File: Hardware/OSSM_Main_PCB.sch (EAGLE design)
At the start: 11 parts, among them J1 PJ-037AH, U1 LOLIN32_PRODUCTION

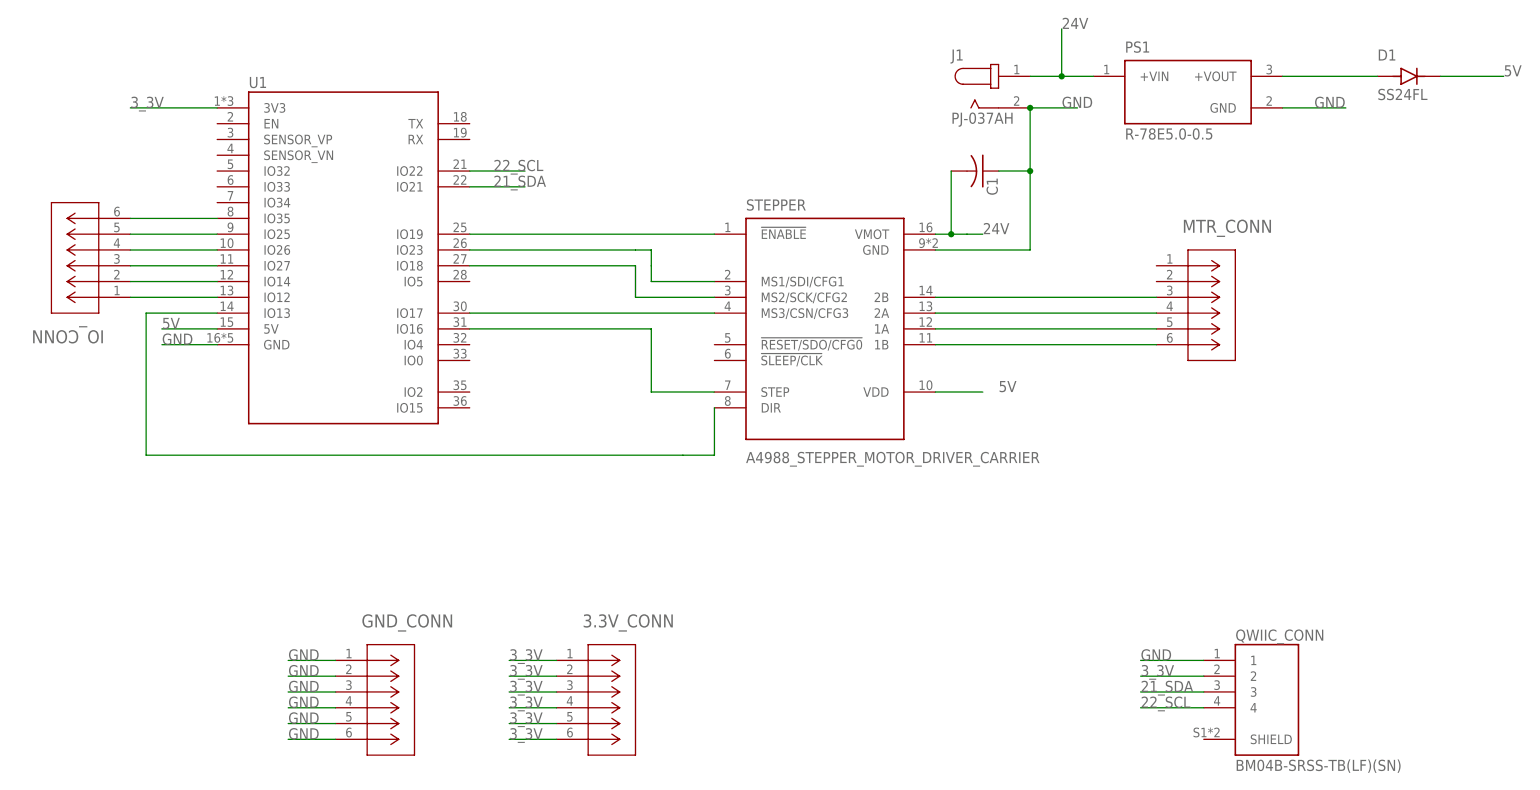
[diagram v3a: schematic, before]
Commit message: Added holes, fixed 3.3V VIO
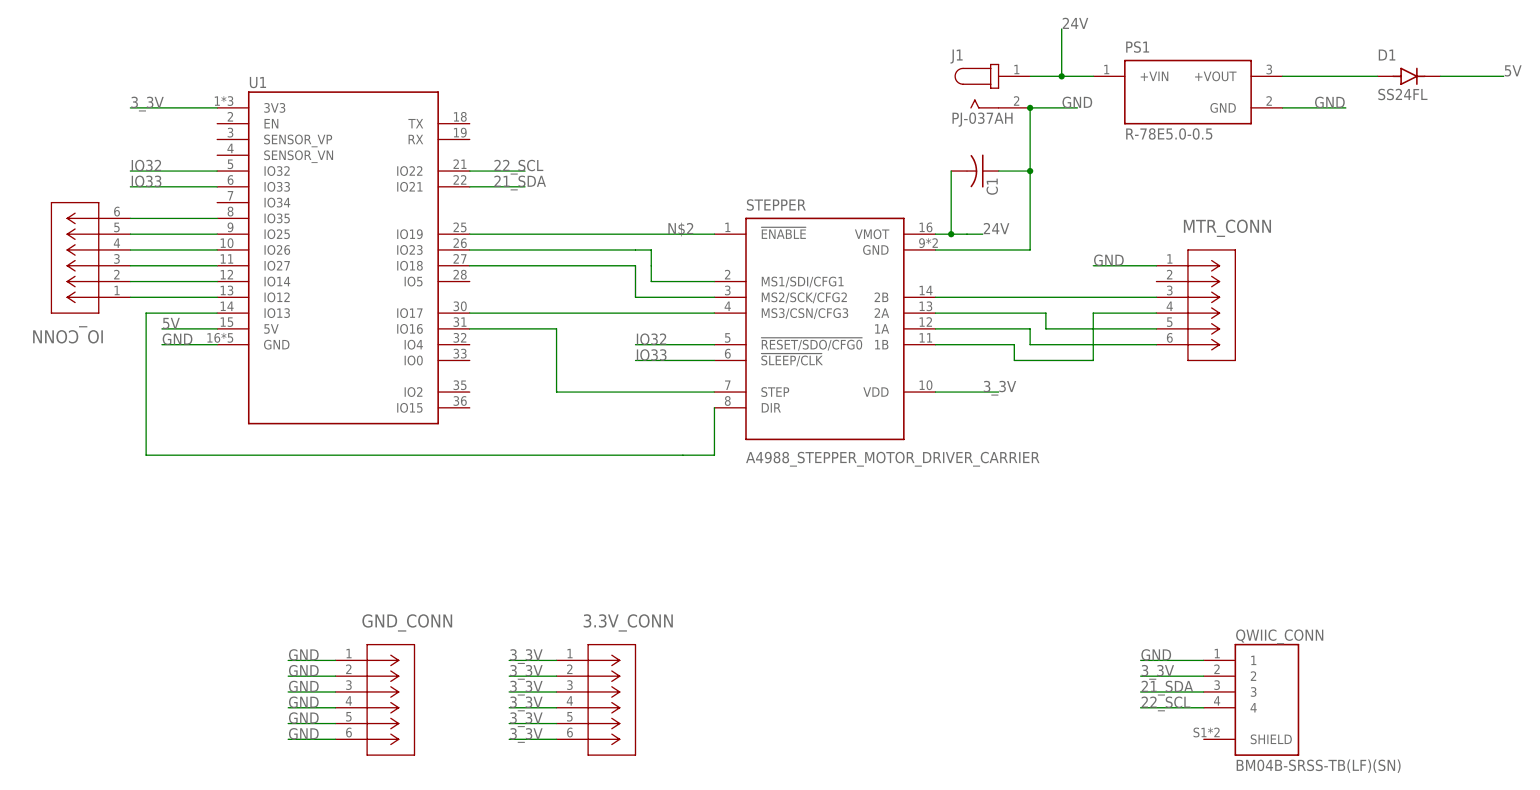
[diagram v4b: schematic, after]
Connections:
- new net IO32: STEPPER.!RESET/SDO/CFG0, U1.IO32
- new net IO33: STEPPER.!SLEEP/CLK, U1.IO33
- net 3_3V: now also STEPPER.VDD
- net 5V: no longer STEPPER.VDD
- net GND: now also MTR_CONN.1
- net N$10: now also STEPPER.1B; no longer STEPPER.2A
- net N$8: now also STEPPER.1A; no longer STEPPER.1B
- net N$9: now also STEPPER.2A; no longer STEPPER.1A
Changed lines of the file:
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@@
 <?xml version="1.0" encoding="utf-8"?>
 <!DOCTYPE eagle SYSTEM "eagle.dtd">
-<eagle version="9.6.2">
+<eagle version="9.6.1">
 <drawing>
 <settings>
@@
 <label x="213.36" y="154.94" size="1.778" layer="95"/>
 </segment>
+<segment>
+<pinref part="MTR_CONN" gate="A" pin="1"/>
+<wire x1="187.96" y1="129.54" x2="177.8" y2="129.54" width="0.1524" layer="91"/>
+<label x="177.8" y="129.54" size="1.778" layer="95"/>
+</segment>
 </net>
 <net name="3_3V" class="0">
@@
 <wire x1="36.83" y1="154.94" x2="22.86" y2="154.94" width="0.1524" layer="91"/>
 <label x="22.86" y="154.94" size="1.778" layer="95"/>
+</segment>
+<segment>
+<pinref part="STEPPER" gate="G$1" pin="VDD"/>
+<wire x1="152.4" y1="109.22" x2="162.56" y2="109.22" width="0.1524" layer="91"/>
+<label x="160.02" y="109.22" size="1.778" layer="95"/>
 </segment>
 </net>
@@
 <label x="27.94" y="119.38" size="1.778" layer="95"/>
 </segment>
-<segment>
-<pinref part="STEPPER" gate="G$1" pin="VDD"/>
-<wire x1="152.4" y1="109.22" x2="160.02" y2="109.22" width="0.1524" layer="91"/>
-<label x="162.56" y="109.22" size="1.778" layer="95"/>
-</segment>
 </net>
 <net name="N$2" class="0">
@@
 <pinref part="STEPPER" gate="G$1" pin="!ENABLE"/>
 <wire x1="77.47" y1="134.62" x2="116.84" y2="134.62" width="0.1524" layer="91"/>
+<label x="109.22" y="134.62" size="1.778" layer="95"/>
 </segment>
 </net>
@@
 <segment>
 <pinref part="U1" gate="G$1" pin="IO16"/>
-<wire x1="77.47" y1="119.38" x2="106.68" y2="119.38" width="0.1524" layer="91"/>
+<wire x1="77.47" y1="119.38" x2="91.44" y2="119.38" width="0.1524" layer="91"/>
 <pinref part="STEPPER" gate="G$1" pin="STEP"/>
-<wire x1="106.68" y1="119.38" x2="106.68" y2="109.22" width="0.1524" layer="91"/>
-<wire x1="106.68" y1="109.22" x2="116.84" y2="109.22" width="0.1524" layer="91"/>
+<wire x1="91.44" y1="119.38" x2="91.44" y2="109.22" width="0.1524" layer="91"/>
+<wire x1="91.44" y1="109.22" x2="116.84" y2="109.22" width="0.1524" layer="91"/>
 </segment>
 </net>
@@
 </segment>
 </net>
-<net name="N$8" class="0">
-<segment>
-<pinref part="STEPPER" gate="G$1" pin="1B"/>
-<pinref part="MTR_CONN" gate="A" pin="6"/>
-<wire x1="152.4" y1="116.84" x2="187.96" y2="116.84" width="0.1524" layer="91"/>
-</segment>
-</net>
-<net name="N$9" class="0">
-<segment>
-<pinref part="MTR_CONN" gate="A" pin="5"/>
-<pinref part="STEPPER" gate="G$1" pin="1A"/>
-<wire x1="187.96" y1="119.38" x2="152.4" y2="119.38" width="0.1524" layer="91"/>
-</segment>
-</net>
-<net name="N$10" class="0">
-<segment>
-<pinref part="STEPPER" gate="G$1" pin="2A"/>
-<pinref part="MTR_CONN" gate="A" pin="4"/>
-<wire x1="152.4" y1="121.92" x2="187.96" y2="121.92" width="0.1524" layer="91"/>
-</segment>
-</net>
 <net name="N$11" class="0">
 <segment>
@@
 </segment>
 </net>
+<net name="IO33" class="0">
+<segment>
+<pinref part="U1" gate="G$1" pin="IO33"/>
+<wire x1="36.83" y1="142.24" x2="22.86" y2="142.24" width="0.1524" layer="91"/>
+<label x="22.86" y="142.24" size="1.778" layer="95"/>
+</segment>
+<segment>
+<pinref part="STEPPER" gate="G$1" pin="!SLEEP/CLK"/>
+<wire x1="116.84" y1="114.3" x2="104.14" y2="114.3" width="0.1524" layer="91"/>
+<label x="104.14" y="114.3" size="1.778" layer="95"/>
+</segment>
+</net>
+<net name="IO32" class="0">
+<segment>
+<pinref part="U1" gate="G$1" pin="IO32"/>
+<wire x1="36.83" y1="144.78" x2="22.86" y2="144.78" width="0.1524" layer="91"/>
+<label x="22.86" y="144.78" size="1.778" layer="95"/>
+</segment>
+<segment>
+<pinref part="STEPPER" gate="G$1" pin="!RESET/SDO/CFG0"/>
+<wire x1="116.84" y1="116.84" x2="104.14" y2="116.84" width="0.1524" layer="91"/>
+<label x="104.14" y="116.84" size="1.778" layer="95"/>
+</segment>
+</net>
+<net name="N$8" class="0">
+<segment>
+<pinref part="STEPPER" gate="G$1" pin="1A"/>
+<wire x1="152.4" y1="119.38" x2="167.64" y2="119.38" width="0.1524" layer="91"/>
+<wire x1="167.64" y1="119.38" x2="167.64" y2="116.84" width="0.1524" layer="91"/>
+<pinref part="MTR_CONN" gate="A" pin="6"/>
+<wire x1="167.64" y1="116.84" x2="187.96" y2="116.84" width="0.1524" layer="91"/>
+</segment>
+</net>
+<net name="N$9" class="0">
+<segment>
+<pinref part="STEPPER" gate="G$1" pin="2A"/>
+<wire x1="152.4" y1="121.92" x2="170.18" y2="121.92" width="0.1524" layer="91"/>
+<wire x1="170.18" y1="121.92" x2="170.18" y2="119.38" width="0.1524" layer="91"/>
+<pinref part="MTR_CONN" gate="A" pin="5"/>
+<wire x1="170.18" y1="119.38" x2="187.96" y2="119.38" width="0.1524" layer="91"/>
+</segment>
+</net>
+<net name="N$10" class="0">
+<segment>
+<wire x1="177.8" y1="114.3" x2="177.8" y2="121.92" width="0.1524" layer="91"/>
+<pinref part="MTR_CONN" gate="A" pin="4"/>
+<wire x1="177.8" y1="121.92" x2="187.96" y2="121.92" width="0.1524" layer="91"/>
+<pinref part="STEPPER" gate="G$1" pin="1B"/>
+<wire x1="152.4" y1="116.84" x2="165.1" y2="116.84" width="0.1524" layer="91"/>
+<wire x1="165.1" y1="116.84" x2="165.1" y2="114.3" width="0.1524" layer="91"/>
+<wire x1="165.1" y1="114.3" x2="177.8" y2="114.3" width="0.1524" layer="91"/>
+</segment>
+</net>

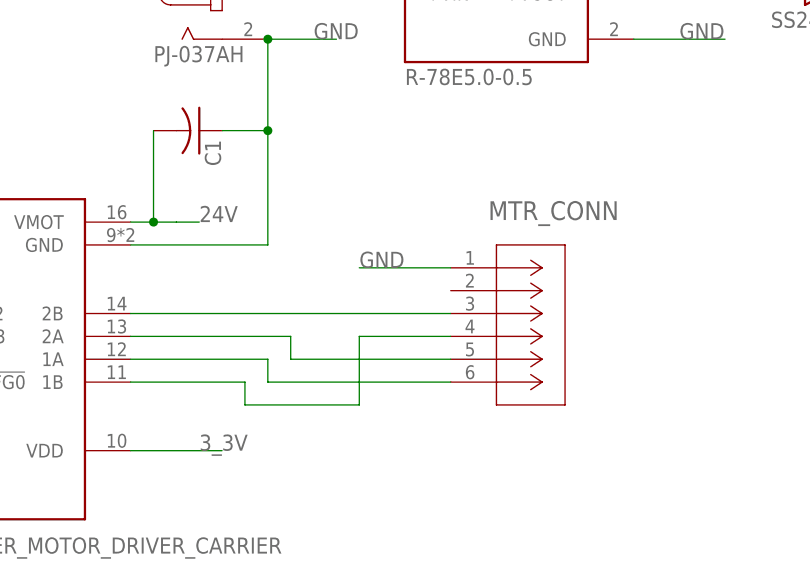
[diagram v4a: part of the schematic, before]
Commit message: Motor 24v + KM marking
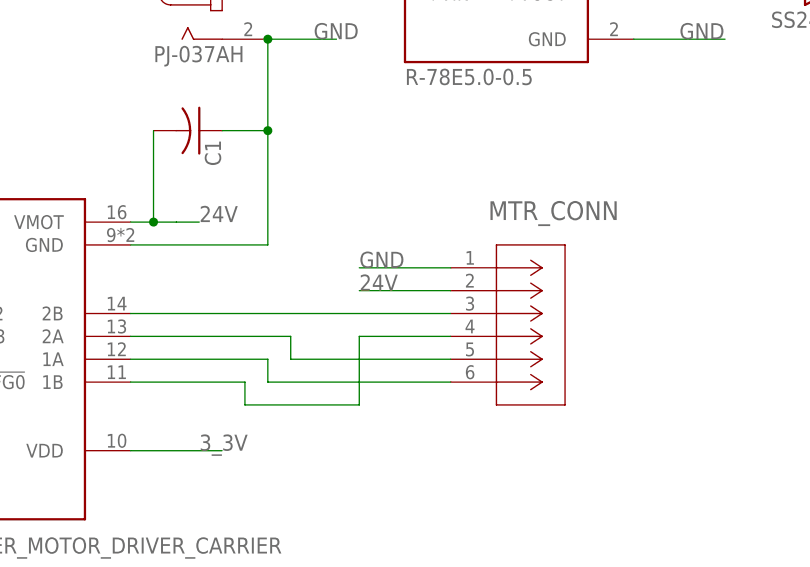
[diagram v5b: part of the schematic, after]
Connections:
- net 24V: now also MTR_CONN.2
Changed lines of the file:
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@@
 <?xml version="1.0" encoding="utf-8"?>
 <!DOCTYPE eagle SYSTEM "eagle.dtd">
-<eagle version="9.6.1">
+<eagle version="9.6.2">
 <drawing>
 <settings>
@@
 <junction x="154.94" y="134.62"/>
 </segment>
+<segment>
+<pinref part="MTR_CONN" gate="A" pin="2"/>
+<wire x1="187.96" y1="127" x2="177.8" y2="127" width="0.1524" layer="91"/>
+<label x="177.8" y="127" size="1.778" layer="95"/>
+</segment>
 </net>

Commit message: changes from initial PCB
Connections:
- net N$10: now also STEPPER.2A; no longer STEPPER.1B
- net N$8: now also STEPPER.1B; no longer STEPPER.1A
- net N$9: now also STEPPER.1A; no longer STEPPER.2A
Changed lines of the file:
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@@
-</segment>
-</net>
-<net name="N$11" class="0">
-<segment>
-<pinref part="MTR_CONN" gate="A" pin="3"/>
-<pinref part="STEPPER" gate="G$1" pin="2B"/>
-<wire x1="187.96" y1="124.46" x2="152.4" y2="124.46" width="0.1524" layer="91"/>
 </segment>
 </net>
@@
 <net name="N$8" class="0">
 <segment>
-<pinref part="STEPPER" gate="G$1" pin="1A"/>
-<wire x1="152.4" y1="119.38" x2="167.64" y2="119.38" width="0.1524" layer="91"/>
-<wire x1="167.64" y1="119.38" x2="167.64" y2="116.84" width="0.1524" layer="91"/>
+<pinref part="STEPPER" gate="G$1" pin="1B"/>
 <pinref part="MTR_CONN" gate="A" pin="6"/>
-<wire x1="167.64" y1="116.84" x2="187.96" y2="116.84" width="0.1524" layer="91"/>
+<wire x1="152.4" y1="116.84" x2="187.96" y2="116.84" width="0.1524" layer="91"/>
 </segment>
 </net>
 <net name="N$9" class="0">
 <segment>
-<pinref part="STEPPER" gate="G$1" pin="2A"/>
-<wire x1="152.4" y1="121.92" x2="170.18" y2="121.92" width="0.1524" layer="91"/>
-<wire x1="170.18" y1="121.92" x2="170.18" y2="119.38" width="0.1524" layer="91"/>
+<pinref part="STEPPER" gate="G$1" pin="1A"/>
 <pinref part="MTR_CONN" gate="A" pin="5"/>
-<wire x1="170.18" y1="119.38" x2="187.96" y2="119.38" width="0.1524" layer="91"/>
+<wire x1="152.4" y1="119.38" x2="187.96" y2="119.38" width="0.1524" layer="91"/>
 </segment>
 </net>
 <net name="N$10" class="0">
 <segment>
-<wire x1="177.8" y1="114.3" x2="177.8" y2="121.92" width="0.1524" layer="91"/>
+<pinref part="STEPPER" gate="G$1" pin="2A"/>
 <pinref part="MTR_CONN" gate="A" pin="4"/>
-<wire x1="177.8" y1="121.92" x2="187.96" y2="121.92" width="0.1524" layer="91"/>
-<pinref part="STEPPER" gate="G$1" pin="1B"/>
-<wire x1="152.4" y1="116.84" x2="165.1" y2="116.84" width="0.1524" layer="91"/>
-<wire x1="165.1" y1="116.84" x2="165.1" y2="114.3" width="0.1524" layer="91"/>
-<wire x1="165.1" y1="114.3" x2="177.8" y2="114.3" width="0.1524" layer="91"/>
+<wire x1="152.4" y1="121.92" x2="187.96" y2="121.92" width="0.1524" layer="91"/>
 </segment>
 </net>
+<net name="N$11" class="0">
+<segment>
+<pinref part="STEPPER" gate="G$1" pin="2B"/>
+<pinref part="MTR_CONN" gate="A" pin="3"/>
+<wire x1="152.4" y1="124.46" x2="187.96" y2="124.46" width="0.1524" layer="91"/>
+</segment>
+</net>
